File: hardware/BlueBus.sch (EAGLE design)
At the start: 139 parts, among them Q1 NMOSFET-BSS138K, Q2 PMOSFET-DMP32D4S, Q3 NMOSFET-BSS138K, X1 CRYSTAL-12MHZ

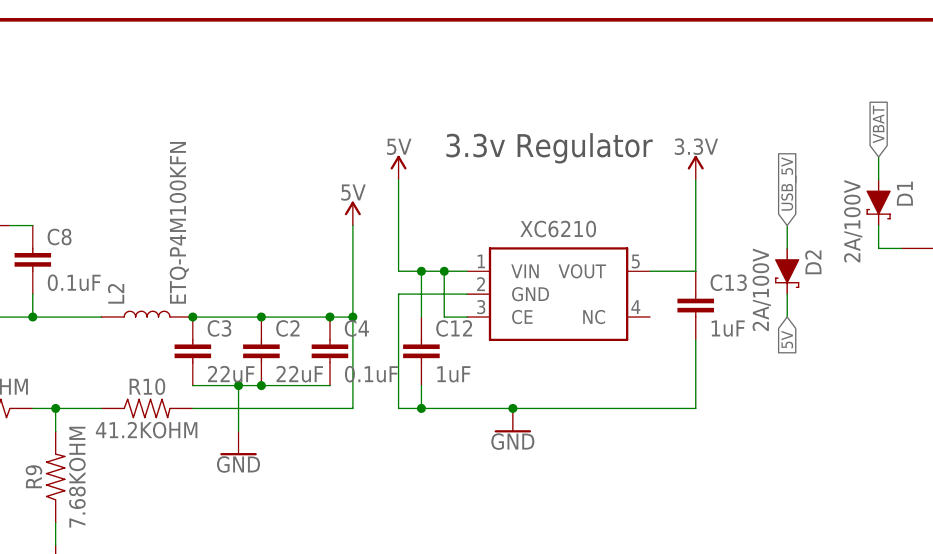
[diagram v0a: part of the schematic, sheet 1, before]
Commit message: [IMP] harware: v1.5 updates * Replace L2 with MPL-SE5040-100 as other part is OOS * Replace C12 and C13 with 22uF capacitors * Replace 22uF capacitor part with one rated for 16v
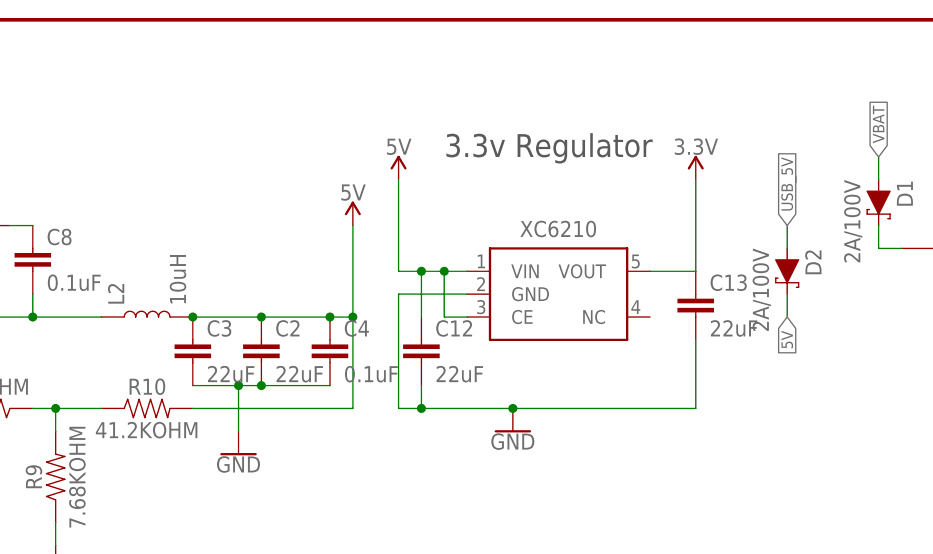
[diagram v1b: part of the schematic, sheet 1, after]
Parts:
- C12, C13: value 1uF -> 22uF; device Passives:1UF -> Passives:22UF
- L2: value ETQ-P4M100KFN -> 10uH; device Passives:ETQ-P4M100KFN -> Passives:MPL-SE5040-100
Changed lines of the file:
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@@
 <part name="D1" library="Passives" deviceset="SCHOTTKYDIODE2A100V" device="" value="2A/100V"/>
 <part name="C3" library="Passives" deviceset="22UF" device="" value="22uF"/>
-<part name="C12" library="Passives" deviceset="1UF" device="" value="1uF"/>
+<part name="C12" library="Passives" deviceset="22UF" device="" value="22uF"/>
 <part name="SUPPLY1" library="SparkFun-PowerSymbols" library_urn="urn:adsk.eagle:library:530" deviceset="VIN" device=""/>
 <part name="GND1" library="SparkFun-PowerSymbols" library_urn="urn:adsk.eagle:library:530" deviceset="GND" device=""/>
-<part name="C13" library="Passives" deviceset="1UF" device="" value="1uF"/>
+<part name="C13" library="Passives" deviceset="22UF" device="" value="22uF"/>
 <part name="SUPPLY3" library="SparkFun-PowerSymbols" library_urn="urn:adsk.eagle:library:530" deviceset="5V" device=""/>
 <part name="C17" library="Passives" deviceset="0.1UF" device="" value="0.1uF"/>
@@
 <part name="R10" library="Passives" deviceset="41.2KOHM" device=""/>
 <part name="C2" library="Passives" deviceset="22UF" device="" value="22uF"/>
-<part name="L2" library="Passives" deviceset="ETQ-P4M100KFN" device=""/>
+<part name="L2" library="Passives" deviceset="MPL-SE5040-100" device="" value="10uH"/>
 <part name="C4" library="Passives" deviceset="0.1UF" device="" value="0.1uF"/>
 <part name="C1" library="Passives" deviceset="RHS1V101MCN1GS" device=""/>
@@
 <attribute name="VALUE" x="98.044" y="145.161" size="1.778" layer="96" font="vector"/>
 </instance>
-<instance part="L2" gate="A" x="83.82" y="152.4" smashed="yes" rot="R90">
+<instance part="L2" gate="G$1" x="83.82" y="152.4" smashed="yes" rot="R90">
 <attribute name="NAME" x="81.28" y="153.67" size="1.778" layer="95" font="vector" rot="R90"/>
 <attribute name="VALUE" x="86.36" y="153.67" size="1.778" layer="96" font="vector" rot="R90" align="top-left"/>
@@
 <wire x1="106.68" y1="162.56" x2="106.68" y2="152.4" width="0.1524" layer="91"/>
 <junction x="106.68" y="152.4"/>
-<pinref part="L2" gate="A" pin="2"/>
+<pinref part="L2" gate="G$1" pin="2"/>
 <junction x="88.9" y="152.4"/>
 <pinref part="C4" gate="G$1" pin="1"/>
@@
 <wire x1="71.12" y1="152.4" x2="78.74" y2="152.4" width="0.1524" layer="91"/>
 <junction x="71.12" y="152.4"/>
-<pinref part="L2" gate="A" pin="1"/>
-</segment>
-</net>
+<pinref part="L2" gate="G$1" pin="1"/>
+</segment>
+</net>
